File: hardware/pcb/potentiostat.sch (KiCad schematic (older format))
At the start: 13 parts

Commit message: Added ad8250 programmable instrumentation amplifier for scalable DAC output.
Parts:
- removed C? (x2): C, ~, symbol C
- added C? (x4): C, ~, symbol C
- added C? (x2): CP1, ~, symbol CP1
- added C? (x2): 10uF, ~, symbol CP1
- added U?: AD8250, ~, symbol AD8250
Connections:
- net labels added: DAC_BIP, DAC_BIP_NX, DAC_GAIN_A0, DAC_GAIN_A1, DAC_UNI, GND
- net labels removed: DAC
- wire segments 39 -> 78
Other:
- note added: "Gain is selected using digital outputs DAC_GAIN_A0 AND DAC_GAIN_A1."
- note added: "Maybe change this to the LT1995? can get gain of 1.67 no need to bias resistors, etc."
- note added: "Scale bipolar DAC (DAC_BIP) by gain N=1,2,5, or 10 to get DAC_BIP_NX."
- note added: "Shifts and scales unipolar DAC (DAC_UNI) from [0V,1.2V] range to bipolar DAC (DAC_BIP) in [-1V,1V] range. \n"
- note added: "Voltage Reference, 0.6V, Tol. 0.5%. Used in when shifting DAC_UNI to DAC_BIP."
- note removed: "0.6V Reference Voltage Tol. 0.5%"
- note removed: "Level shift and scaling of [0, 1.2V] DAC output to [-1,1]"
- moved on the sheet: C?, R?, U?

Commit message: Added +/- 15V supply for op amps.  Added programmable gain amplifiers.
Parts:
- removed C? (x2): C, ~, symbol C
- removed C?: CP1, ~, symbol CP1
- removed C?: 10uF, ~, symbol CP1
- removed R? (x4): R, ~, symbol R
- removed U? (x2): OP07, ~, symbol OP07
- added C? (x2): 0.1uF, ~, symbol C
- added C? (x2): 10uF, ~, symbol CP1
- added U?: LT1995, ~, symbol LT1995
- added U?: MEA1D05XXSC, ~, symbol MEA1D05XXSC
- C? (x2): value C -> 10nF
- C?: value CP1 -> 4.7uf
- C?: value 10uF -> 4.7uF
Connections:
- net labels added: +15V, -15V, 5V
- wire segments 78 -> 84
- no-connect marks 3 -> 1
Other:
- note added: "+/- 15V Supply for OPAMPs"
- note added: "Gain=1.67"
- note removed: "Maybe change this to the LT1995? can get gain of 1.67 no need to bias resistors, etc."
- moved on the sheet: C?, R?, U?

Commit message: More work on design.
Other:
- note added: "Amplifier Gain=1.67"
- note added: "Scales bipolar DAC (DAC_BIP) by gain N=1,2,5, or 10 to get DAC_BIP_NX."
- note removed: "Gain=1.67"
- note removed: "Scale bipolar DAC (DAC_BIP) by gain N=1,2,5, or 10 to get DAC_BIP_NX."
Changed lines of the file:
@@
 +15V
 Text Notes 925  6700 0    60   ~ 0
-Scale bipolar DAC (DAC_BIP) by gain N=1,2,5, or 10 to get DAC_BIP_NX.
+Scales bipolar DAC (DAC_BIP) by gain N=1,2,5, or 10 to get DAC_BIP_NX.
 Text Notes 925  6850 0    60   ~ 0
 Gain is selected using digital outputs DAC_GAIN_A0 AND DAC_GAIN_A1.
@@
 +15V
 Text Notes 3450 4850 0    60   ~ 0
-Gain=1.67
+Amplifier Gain=1.67
 $Comp
 L MEA1D05XXSC U?

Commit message: Further work on poteniostat circuit.
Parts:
- added C? (x2): 0.1uF, ~, symbol C
- added C? (x2): 10uF, ~, symbol CP1
- added U? (x2): OPA129, ~, symbol OPA129
- added U?: OPA227, ~, symbol OPA227
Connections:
- net +15V: now also C?.1, C?.1, U?.7 (V+)
- net -15V: now also C?.2, C?.2, U?.5 (V-)
- net AGND: now also C?.1, C?.1, C?.2, C?.2
- new net REF_ELECT: U?.3 (IN+)
- new net REF_ELECT_BUF: U?.1 (NC), U?.2 (IN-), U?.4 (NC), U?.6 (OUT), U?.8 (SUB)
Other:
- note added: "Control Amplifier"
- note added: "Transimpedance Amplifier"
- note added: "Uniy Gain Buffer for Reference Electrode"
- moved on the sheet: C?, R?, U?

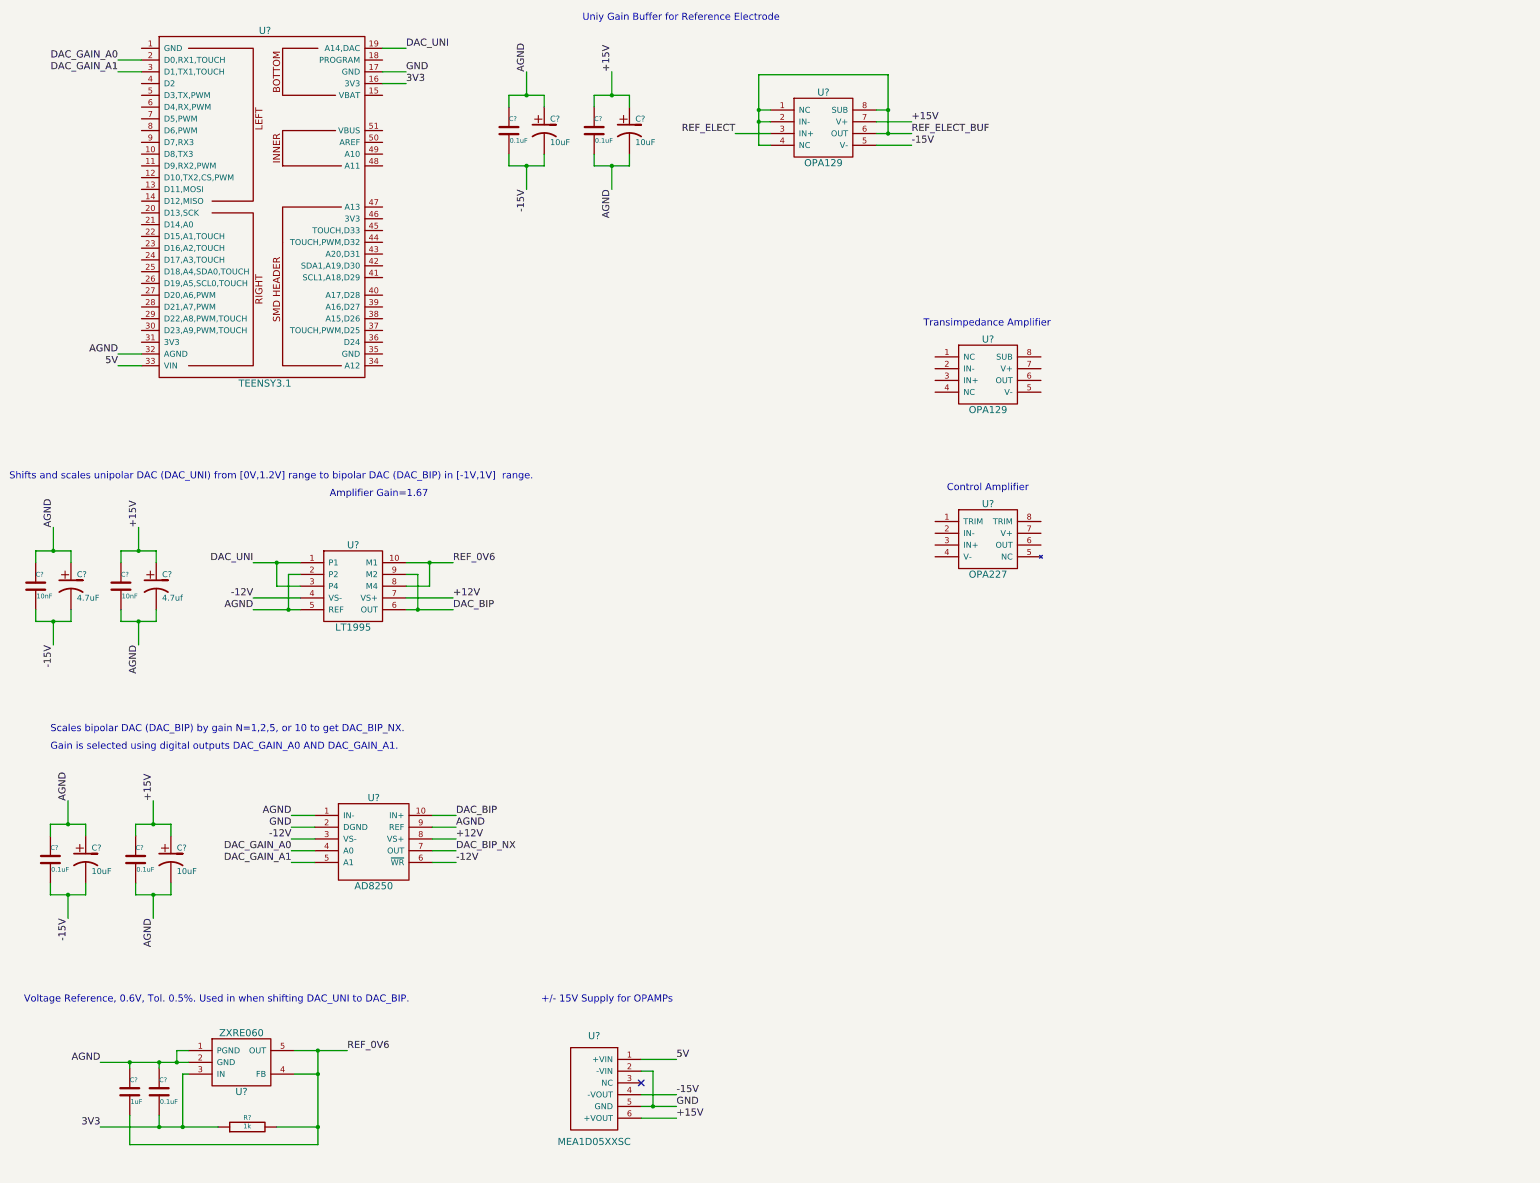
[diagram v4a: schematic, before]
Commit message: Worked more on initial design added programmable gain transimpedance amplifier and expansion header.
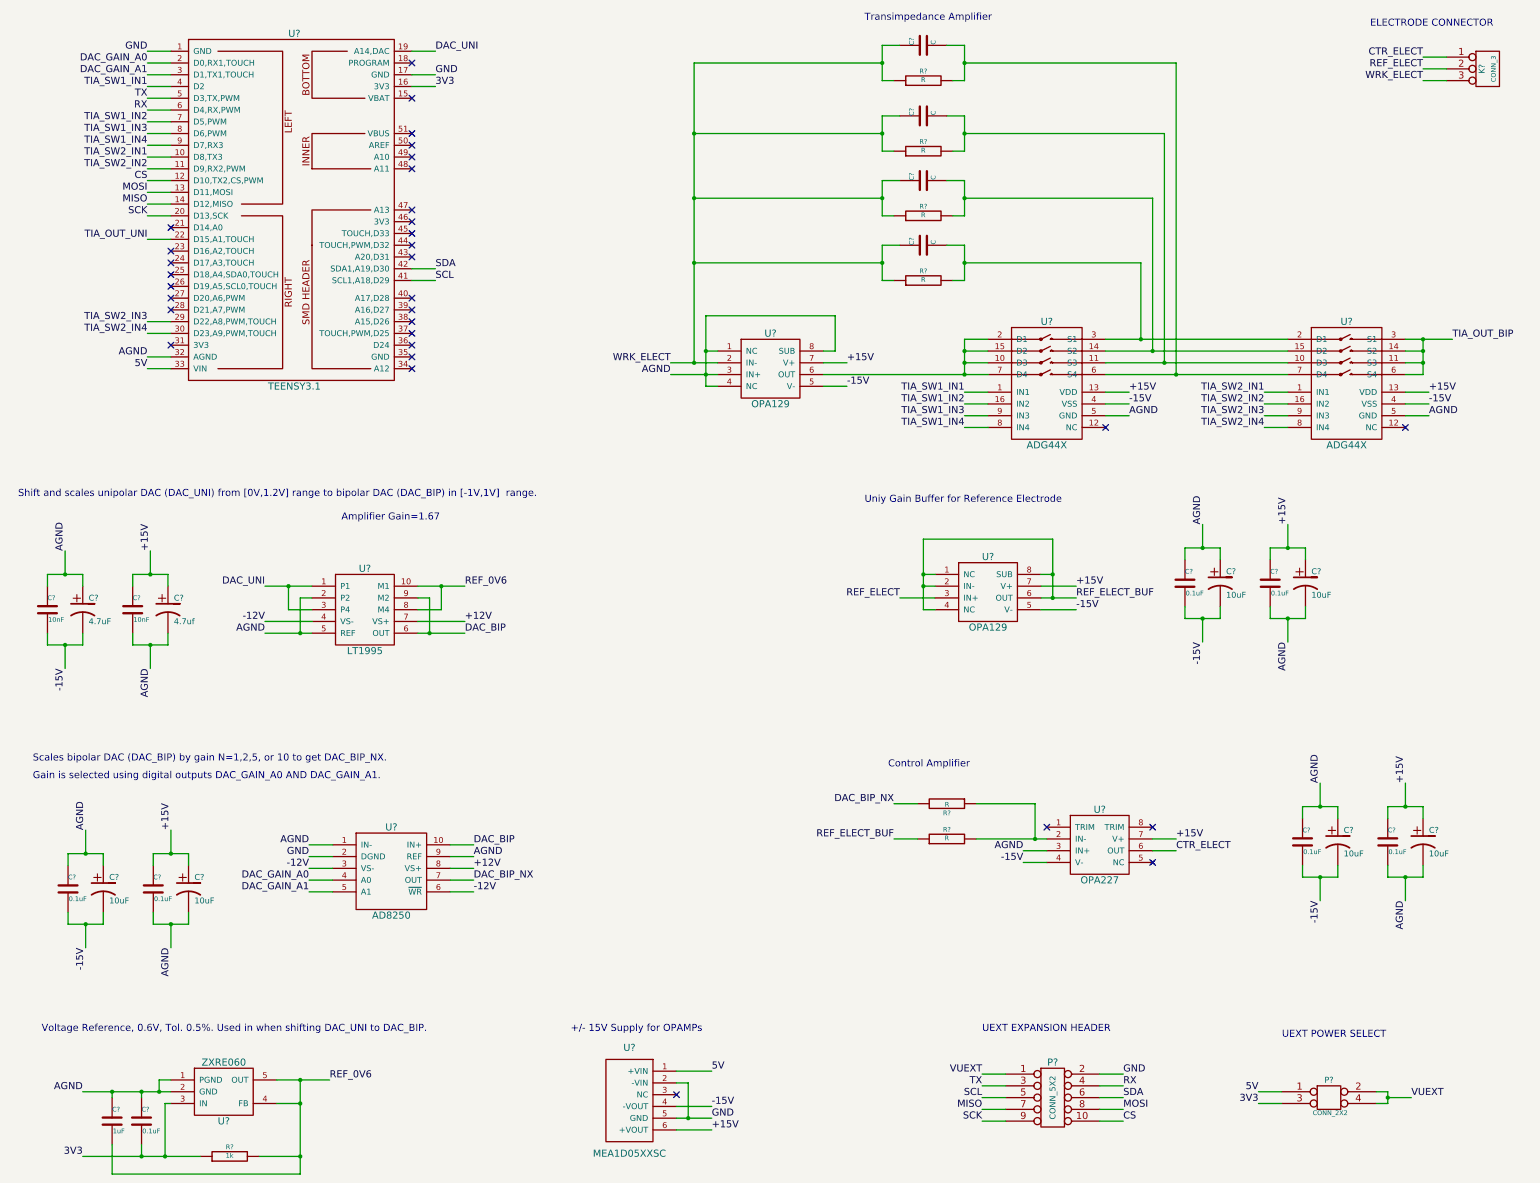
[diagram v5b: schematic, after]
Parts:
- added C? (x2): 0.1uF, ~, symbol C
- added C? (x2): 10uF, ~, symbol CP1
- added C? (x4): C, ~, symbol C
- added K?: CONN_3, symbol CONN_3
- added P?: CONN_5X2, symbol CONN_5X2
- added P?: CONN_2X2, symbol CONN_2X2
- added R? (x6): R, ~, symbol R
- added U? (x2): ADG44X, symbol ADG44X
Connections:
- net +15V: now also U?.7 (V+), U?.7 (V+), C?.1, C?.1, U?.13 (VDD), U?.13 (VDD)
- net -15V: now also U?.4 (V-), U?.5 (V-), C?.2, C?.2, U?.4 (VSS), U?.4 (VSS)
- net 3V3: now also P?.3
- net 5V: now also P?.1
- net AGND: now also U?.1 (NC), U?.3 (IN+), U?.3 (IN+), U?.4 (NC), U?.8 (SUB), C?.1, C?.1, C?.2, C?.2, U?.5 (GND), U?.5 (GND)
- net DAC_BIP_NX: now also R?.2
- net GND: now also U?.1 (GND), P?.2
- net REF_ELECT: now also K?.2 (PM)
- net REF_ELECT_BUF: now also R?.1
- net TIA_SW2_IN1: now reaches U?.10 (D8,TX3)
- net TIA_SW2_IN1: now also U?.1 (IN1)
- net TIA_SW2_IN2: now reaches U?.11 (D9,RX2,PWM)
- net TIA_SW2_IN2: now also U?.16 (IN2)
- net CS: now reaches U?.12 (D10,TX2,CS,PWM)
- net CS: now also P?.10
- net MOSI: now reaches U?.13 (D11,MOSI)
- net MOSI: now also P?.8
- net MISO: now reaches U?.14 (D12,MISO)
- net MISO: now also P?.7
- net SCK: now reaches U?.20 (D13,SCK)
- net SCK: now also P?.9
- net TIA_OUT_UNI: now reaches U?.22 (D15,A1,TOUCH)
- net TIA_SW2_IN3: now reaches U?.29 (D22,A8,PWM,TOUCH)
- net TIA_SW2_IN3: now also U?.9 (IN3)
- net TIA_SW2_IN4: now reaches U?.30 (D23,A9,PWM,TOUCH)
- net TIA_SW2_IN4: now also U?.8 (IN4)
- net TIA_SW1_IN1: now reaches U?.4 (D2)
- net TIA_SW1_IN1: now also U?.1 (IN1)
- net SCL: now reaches U?.41 (SCL1,A18,D29)
- net SCL: now also P?.5
- net SDA: now reaches U?.42 (SDA1,A19,D30)
- net SDA: now also P?.6
- net TX: now reaches U?.5 (D3,TX,PWM)
- net TX: now also P?.3
- net RX: now reaches U?.6 (D4,RX,PWM)
- net RX: now also P?.4
- net TIA_SW1_IN2: now reaches U?.7 (D5,PWM)
- net TIA_SW1_IN2: now also U?.16 (IN2)
- net TIA_SW1_IN3: now reaches U?.8 (D6,PWM)
- net TIA_SW1_IN3: now also U?.9 (IN3)
- net TIA_SW1_IN4: now reaches U?.9 (D7,RX3)
- net TIA_SW1_IN4: now also U?.8 (IN4)
- net WRK_ELECT: now reaches U?.2 (IN-)
- net WRK_ELECT: now also C?.1, C?.1, C?.1, C?.1, K?.3 (P3), R?.1, R?.1, R?.1, R?.1
- net at U?.6 (OUT): now also U?.10 (D3), U?.15 (D2), U?.2 (D1), U?.7 (D4)
- net at U?.2 (IN-): now also R?.1, R?.2
- net CTR_ELECT: now reaches U?.6 (OUT)
- net CTR_ELECT: now also K?.1 (P1)
- new net: C?.2, R?.2, U?.2 (D1), U?.3 (S1)
- new net: C?.2, R?.2, U?.14 (S2), U?.15 (D2)
- new net: C?.2, R?.2, U?.10 (D3), U?.11 (S3)
- new net: C?.2, R?.2, U?.6 (S4), U?.7 (D4)
- new net TIA_OUT_BIP: U?.11 (S3), U?.14 (S2), U?.3 (S1), U?.6 (S4)
- new net VUEXT: P?.1, P?.2, P?.4
- no-connect marks 1 -> 32
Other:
- note added: "ELECTRODE CONNECTOR"
- note added: "Shift and scales unipolar DAC (DAC_UNI) from [0V,1.2V] range to bipolar DAC (DAC_BIP) in [-1V,1V] range. \n"
- note added: "UEXT EXPANSION HEADER"
- note added: "UEXT POWER SELECT"
- note removed: "Shifts and scales unipolar DAC (DAC_UNI) from [0V,1.2V] range to bipolar DAC (DAC_BIP) in [-1V,1V] range. \n"
- moved on the sheet: C?, R?, U?

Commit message: Added level shifter (0.6V) to output of transimpedance amplifier.  Added note on what still needs to be done to complete the design.
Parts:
- added U?: LT1995, ~, symbol LT1995
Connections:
- net +12V is gone; now on net +15V: U?.7 (VS+), U?.8 (VS+)
- net +15V: now also U?.7 (VS+)
- net -12V: no longer U?.3 (VS-), U?.4 (VS-)
- net -15V: now also U?.3 (VS-), U?.4 (VS-), U?.4 (VS-)
- net AGND: now also U?.5 (REF)
- net REF_0V6: now also U?.1 (P1)
- net TIA_OUT_BIP: no longer names the net of U?.11 (S3), U?.14 (S2), U?.3 (S1), U?.6 (S4)
- net TIA_OUT_BIP: now also U?.10 (M1)
- net TIA_OUT_UNI renamed TIA_OUT
- net TIA_OUT: now also U?.6 (OUT)
- no-connect marks 32 -> 36
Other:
- note added: "1. Add decoupling caps to ICs in transimpedance amp."
- note added: "2. Add test points for debugging?"
- note added: "3. Edit library pin definitions to so that DRC works correctly."
- note added: "4. Add power flags for DRC works correctly."
- note added: "5. Specify missing component values e.g. transimpedance amplifier Rs and Cs."
- note added: "6. Add input protection (Schottky diode pair?) to TIA_OUT to protect analog input."
- note added: "Electrode Connector"
- note added: "Notes:"
- note added: "Scale bipolar DAC (DAC_BIP) by gain N=1,2,5, or 10 to get DAC_BIP_NX."
- note removed: "ELECTRODE CONNECTOR"
- note removed: "Scales bipolar DAC (DAC_BIP) by gain N=1,2,5, or 10 to get DAC_BIP_NX."
- moved on the sheet: C?, K?, P?, R?, U?

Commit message: Added schottky diode and decoupling caps to TIA.
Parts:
- added C? (x2): 10nF, ~, symbol C
- added C?: 4.7uf, ~, symbol CP1
- added C?: 4.7uF, ~, symbol CP1
- added C? (x2): 0.1uF, ~, symbol C
- added C? (x2): 10uF, ~, symbol CP1
- added C? (x4): C, ~, symbol C
- added D?: BAS07-04, ~, symbol BAS07-04
- added R? (x2): R, ~, symbol R
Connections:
- net +15V: now also C?.1, C?.1, C?.1, C?.1, C?.1, C?.1
- net -15V: now also C?.2, C?.2, C?.2, C?.2, C?.2, C?.2
- net 3V3: now also D?.2 (cathode)
- net AGND: now also C?.1, C?.1, C?.1, C?.1, C?.1, C?.1, C?.2, C?.2, C?.2, C?.2, C?.2, C?.2, D?.1 (Anode)
- net TIA_OUT: now also R?.2; no longer U?.6 (OUT)
- new net: R?.1, U?.6 (OUT)
- new net: D?.3 (AK), R?.1, R?.2
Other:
- note added: "1. Add analog input for reference electrode (buffered). Could just take -[10V, 10V] analog input from noah motion controller."
- note added: "DAC_GAIN_A0 and DAC_GAIN_A1."
- note added: "Scale bipolar DAC (DAC_BIP) by gain N=1,2,5, or 10 to get DAC_BIP_NX. Gain is selected using"
- note removed: "1. Add decoupling caps to ICs in transimpedance amp."
- note removed: "6. Add input protection (Schottky diode pair?) to TIA_OUT to protect analog input."
- note removed: "Gain is selected using digital outputs DAC_GAIN_A0 AND DAC_GAIN_A1."
- note removed: "Scale bipolar DAC (DAC_BIP) by gain N=1,2,5, or 10 to get DAC_BIP_NX."
- moved on the sheet: C?, K?, P?, R?, U?
